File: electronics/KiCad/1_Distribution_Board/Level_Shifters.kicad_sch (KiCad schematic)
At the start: 39 parts, among them J16 Conn_01x02, J2 Conn_01x02, J24 Conn_01x03, J25 Conn_01x03, J26 Conn_01x03, J27 Conn_01x03, Q1 TBD, Q10 2N7000, Q4 TBD, Q6 2N7000, Q7 2N7000, Q8 2N7000, Q9 2N7000

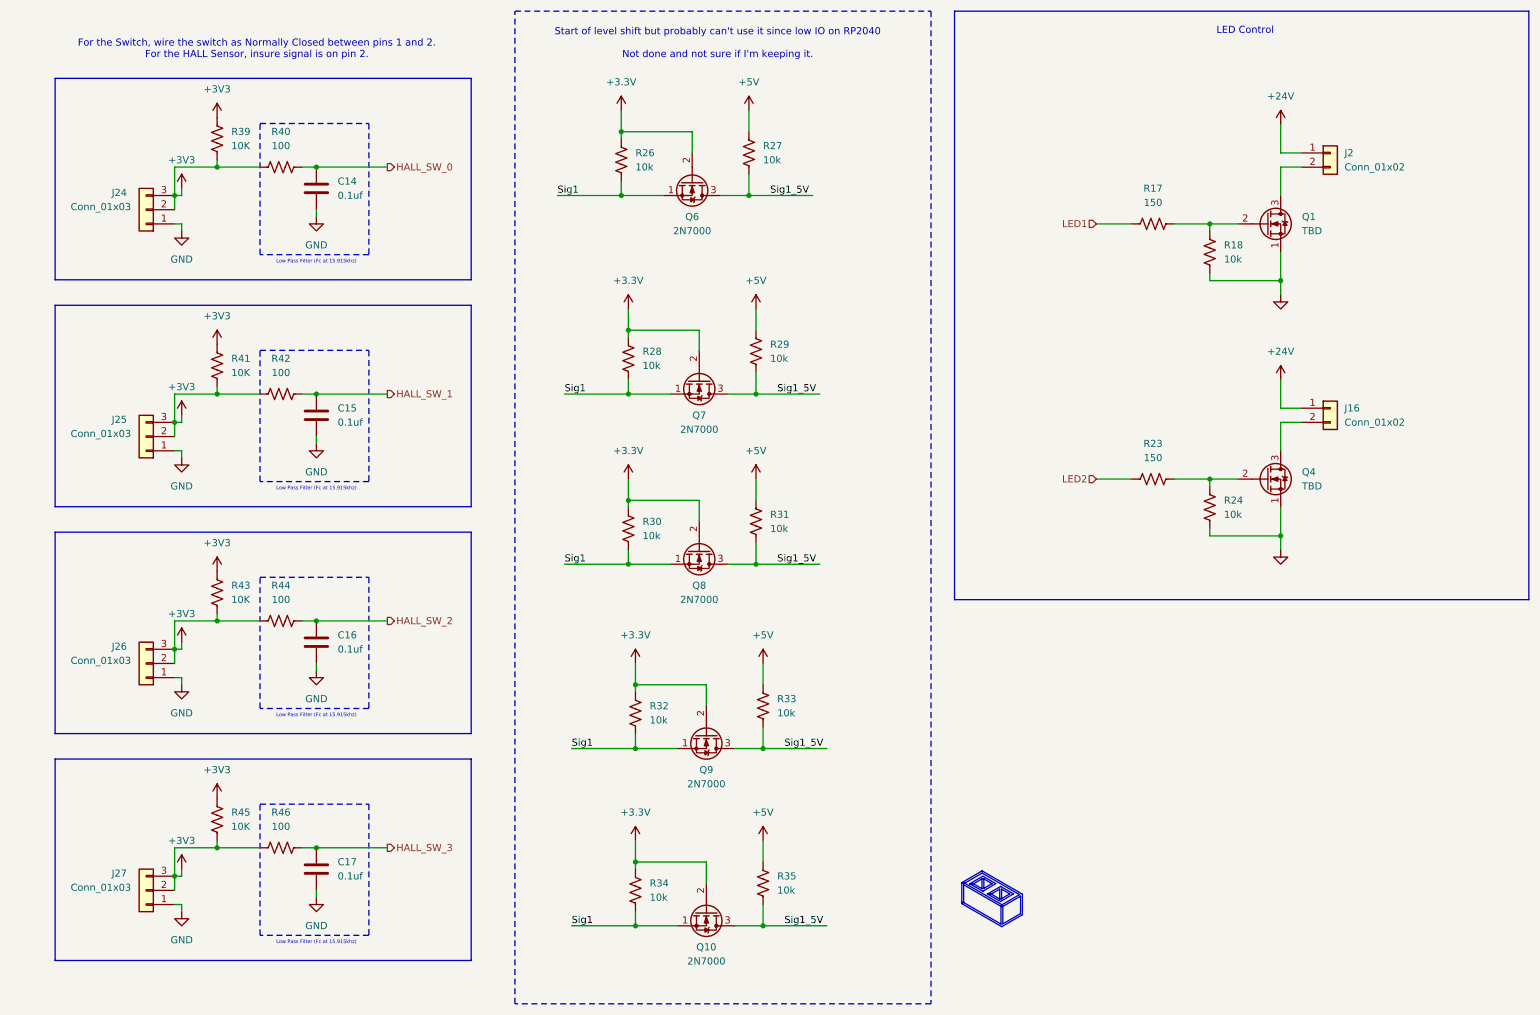
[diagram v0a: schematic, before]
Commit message: Updated schematics
Updated to remove additional stepper drive, corrected short on hall circuit. Removed level shifters for PWM signals.
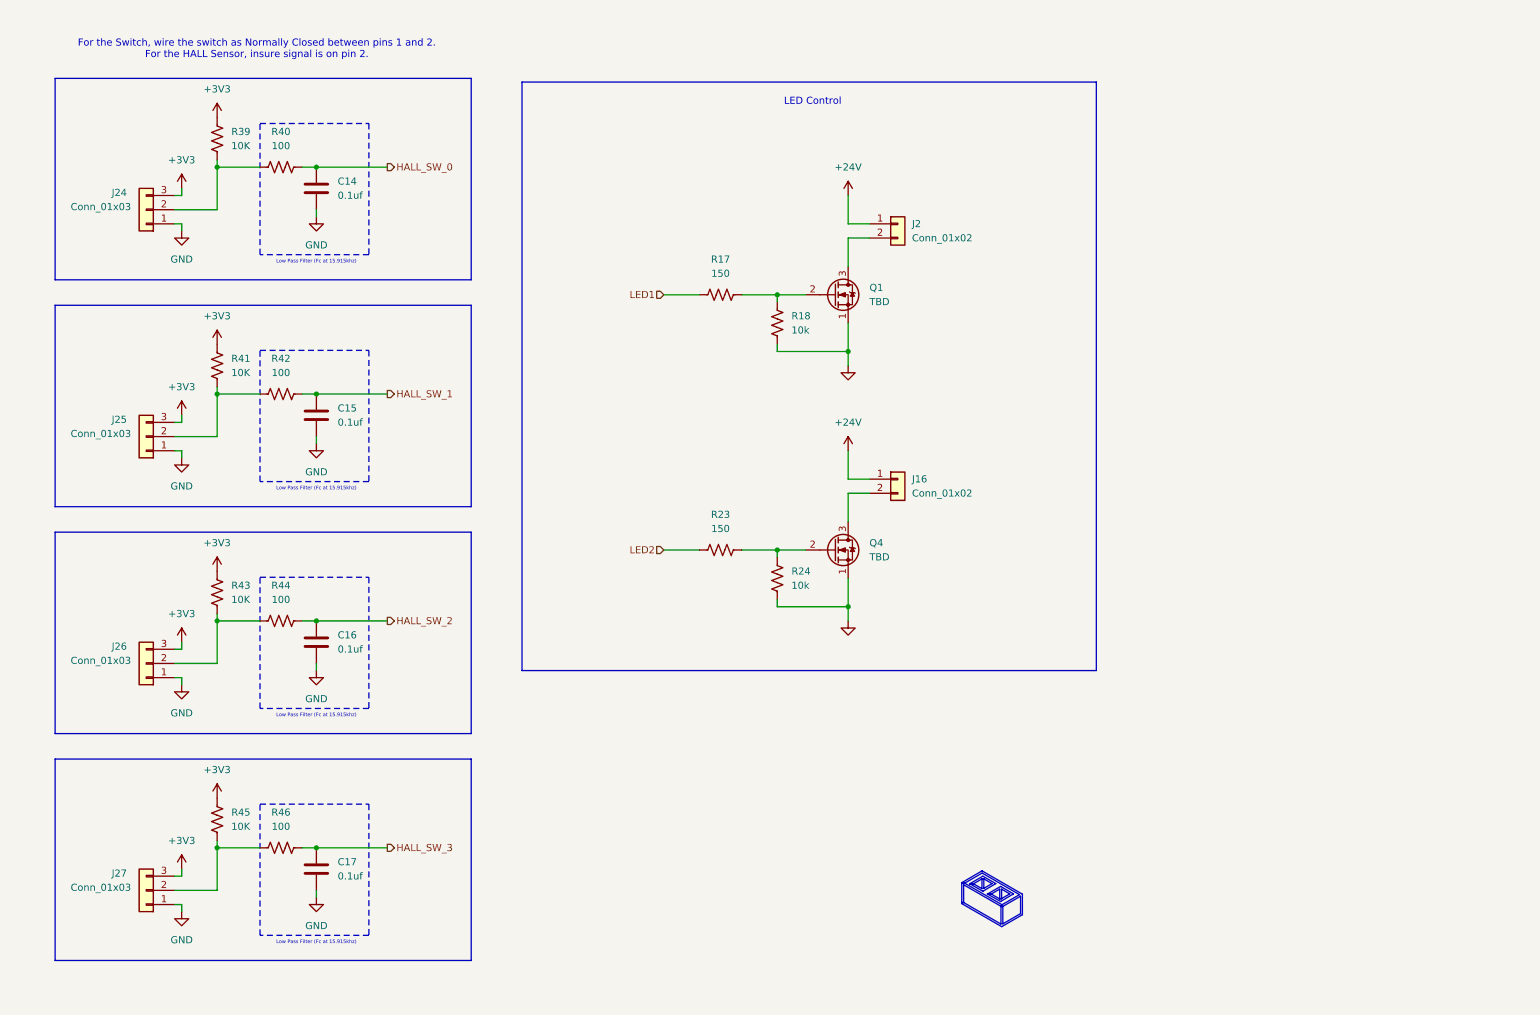
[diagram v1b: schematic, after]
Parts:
- removed Q10, Q6, Q7, Q8, Q9: 2N7000, Package_TO_SOT_THT:TO-92_Inline, symbol Transistor_FET:2N7000
- removed R26, R27, R28, R29, R30, R31, R32, R33, R34, R35: 10k, symbol Device:R_US
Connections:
- net +3V3: no longer J24.2 (Pin_2), J25.2 (Pin_2), J26.2 (Pin_2), J27.2 (Pin_2), R39.2, R40.1, R41.2, R42.1, R43.2, R44.1, R45.2, R46.1
- new net: J25.2 (Pin_2), R41.2, R42.1
- new net: J26.2 (Pin_2), R43.2, R44.1
- new net: J24.2 (Pin_2), R39.2, R40.1
- new net: J27.2 (Pin_2), R45.2, R46.1
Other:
- note removed: "Start of level shift but probably can't use it since low IO on RP2040 Not done and not sure if I'm keeping it."
- moved on the sheet: J16, J2, Q1, Q4, R17, R18, R23, R24

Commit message: footprint additions
Added Footprints to resistors and most components.
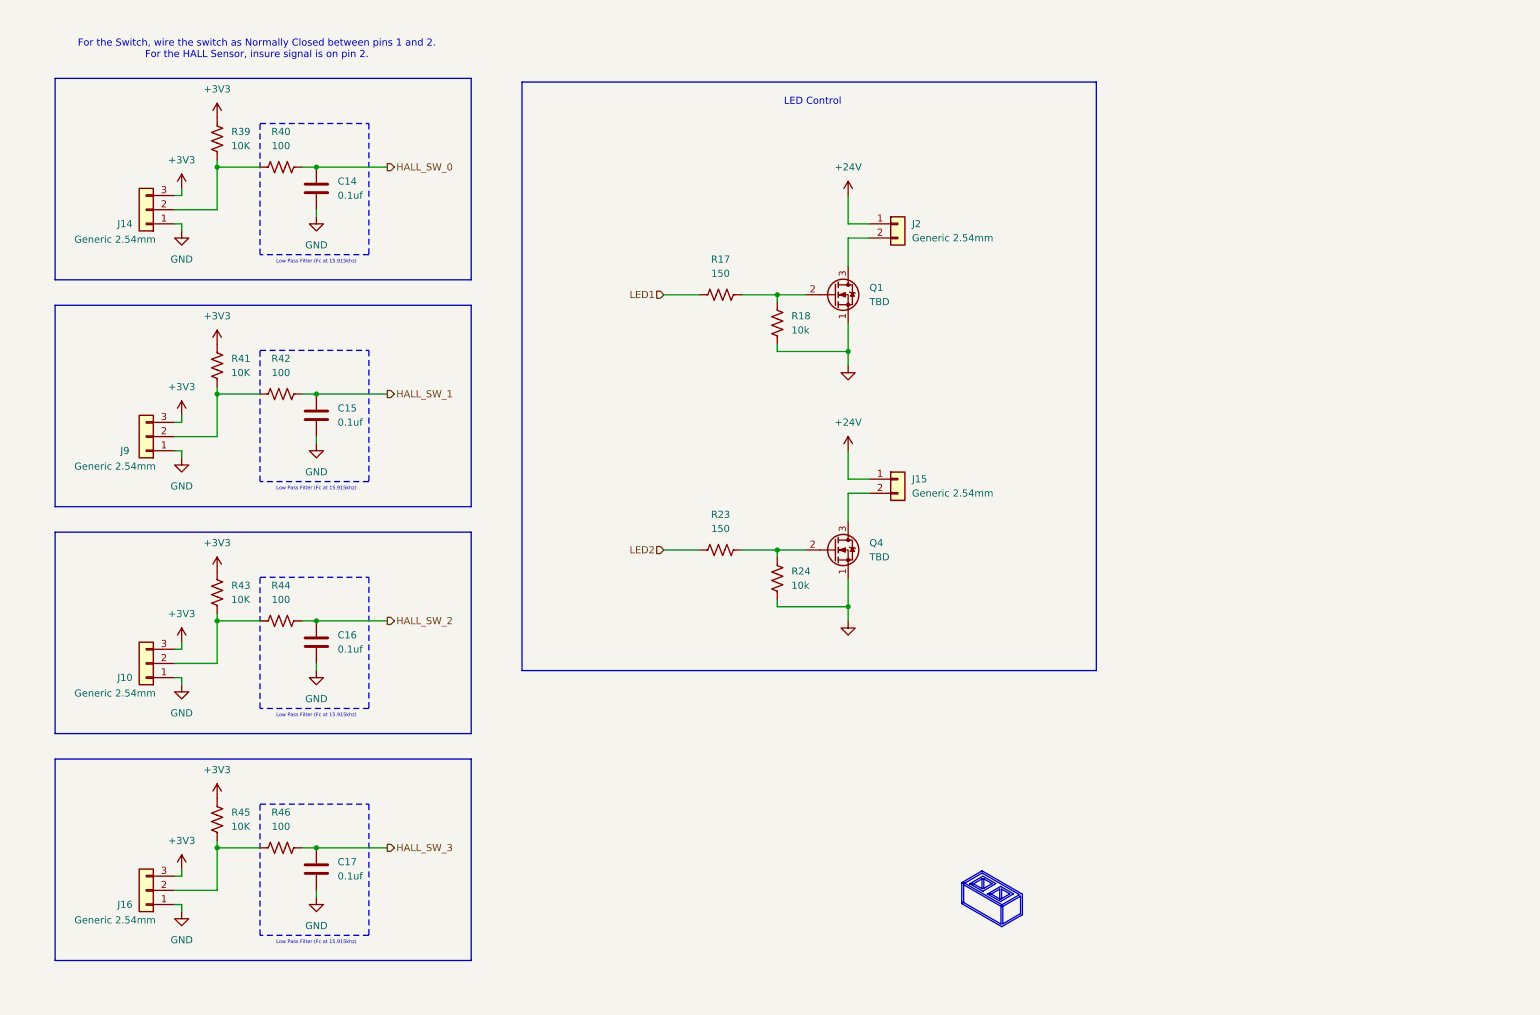
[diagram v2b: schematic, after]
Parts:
- removed J16: Conn_01x02, symbol Connector_Generic:Conn_01x02
- removed J24, J25, J26, J27: Conn_01x03, symbol Connector_Generic:Conn_01x03
- added J10, J14, J16, J9: Generic 2.54mm, Connector_PinHeader_2.54mm:PinHeader_1x03_P2.54mm_Vertical, symbol Connector_Generic:Conn_01x03
- added J15: Generic 2.54mm, Connector_PinHeader_2.54mm:PinHeader_1x02_P2.54mm_Vertical, symbol Connector_Generic:Conn_01x02
- C14, C15, C16, C17: footprint (none) -> Capacitor_SMD:C_0805_2012Metric_Pad1.18x1.45mm_HandSolder
- J2: value Conn_01x02 -> Generic 2.54mm; footprint (none) -> Connector_PinHeader_2.54mm:PinHeader_1x02_P2.54mm_Vertical
- R17, R18, R23, R24, R39, R40, R41, R42, R43, R44, R45, R46: footprint (none) -> Resistor_SMD:R_0805_2012Metric_Pad1.20x1.40mm_HandSolder
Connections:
- net +24V: now also J15.1 (Pin_1)
- net +3V3: now also J10.3 (Pin_3), J14.3 (Pin_3), J16.3 (Pin_3), J9.3 (Pin_3)
- net GND: now also J10.1 (Pin_1), J14.1 (Pin_1), J16.1 (Pin_1), J9.1 (Pin_1)
- net at R41.2, R42.1: now also J9.2 (Pin_2)
- net at R43.2, R44.1: now also J10.2 (Pin_2)
- net at R39.2, R40.1: now also J14.2 (Pin_2)
- net at Q4.3 (D): now also J15.2 (Pin_2)
- net at R45.2, R46.1: now also J16.2 (Pin_2)

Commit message: Updated to add 2 more steppers
Updated to add two more steppers, dual with the motor controllers. they will be either or. Layout hole pattern started. Still need some footprints assigned.
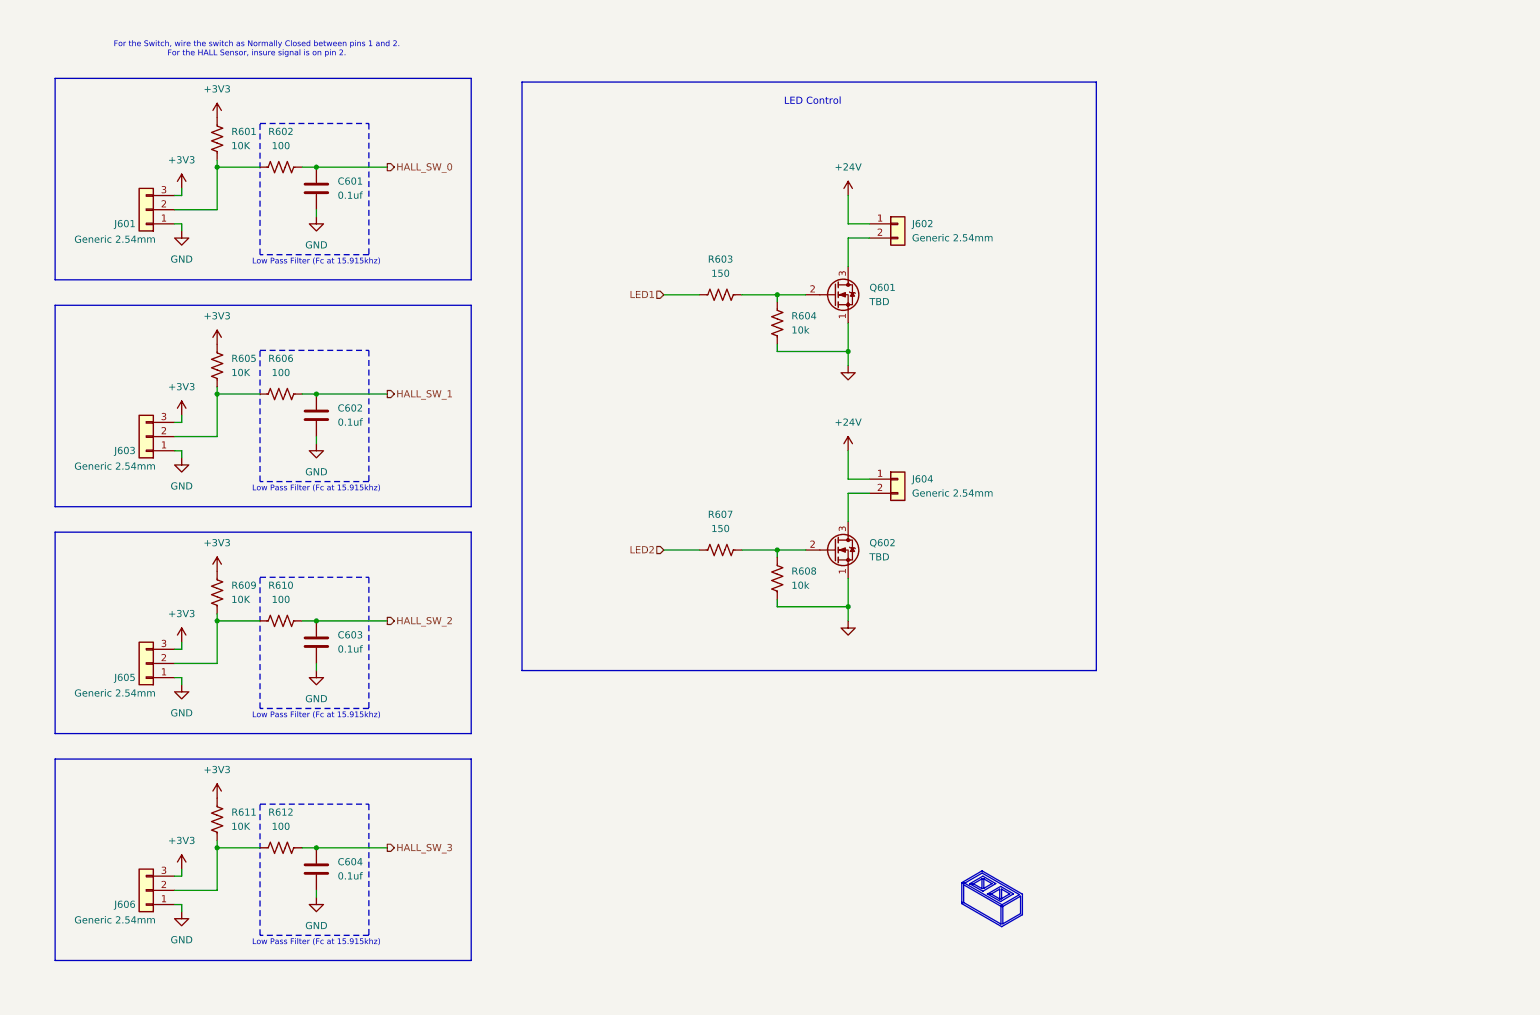
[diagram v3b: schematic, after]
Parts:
- renumbered C14 to C601, C15 to C602, C16 to C603, C17 to C604, J14 to J601, J2 to J602, J9 to J603, J15 to J604, J10 to J605, J16 to J606, Q1 to Q601, Q4 to Q602, R39 to R601, R40 to R602, R17 to R603, R18 to R604, R41 to R605, R42 to R606, R23 to R607, R24 to R608, R43 to R609, R44 to R610, R45 to R611, R46 to R612

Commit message: Added 4th stepper
Added 4th stepper on SCH and PCB
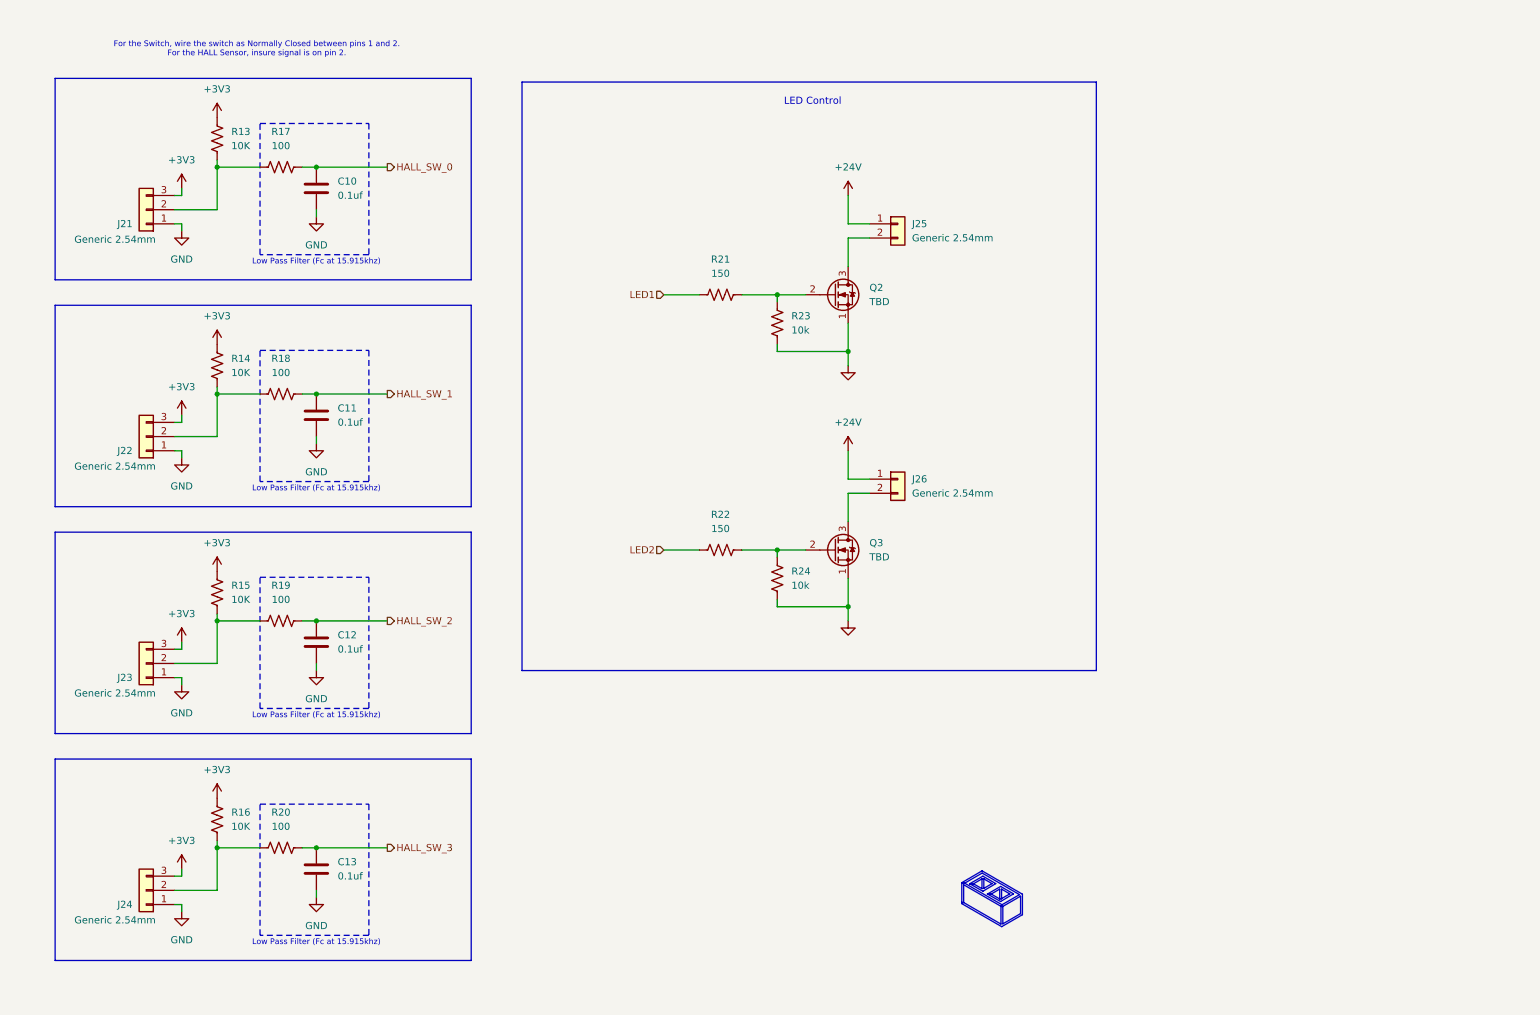
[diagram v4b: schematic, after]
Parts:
- renumbered C601 to C10, C602 to C11, C603 to C12, C604 to C13, J601 to J21, J603 to J22, J605 to J23, J606 to J24, J602 to J25, J604 to J26, Q601 to Q2, Q602 to Q3, R601 to R13, R605 to R14, R609 to R15, R611 to R16, R602 to R17, R606 to R18, R610 to R19, R612 to R20, R603 to R21, R607 to R22, R604 to R23, R608 to R24

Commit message: Updated sch
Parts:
- added J101, J601: Conn_01x04, symbol Connector_Generic:Conn_01x04
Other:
- note added: "NEO Pixel 1"
- note added: "NEO Pixel 2"
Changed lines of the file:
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@@
+	)
+	(rectangle
+		(start 208.915 26.67)
+		(end 278.13 67.31)
+		(stroke
+			(width 0)
+			(type solid)
+		)
+		(fill
+			(type none)
+		)
 	)
 	(rectangle
@@
 			(width 0)
 			(type dot)
+		)
+		(fill
+			(type none)
+		)
+	)
+	(rectangle
+		(start 208.915 69.85)
+		(end 278.13 110.49)
+		(stroke
+			(width 0)
+			(type solid)
 		)
 		(fill
@@
 		)
 	)
+	(text "NEO Pixel 2"
+		(exclude_from_sim no)
+		(at 243.078 75.438 0)
+		(effects
+			(font
+				(size 1.27 1.27)
+			)
+		)
+	)
 	(text "For the Switch, wire the switch as Normally Closed between pins 1 and 2.\nFor the HALL Sensor, insure signal is on pin 2.\n"
 		(exclude_from_sim no)
@@
 			(font
 				(size 1.016 1.016)
+			)
+		)
+	)
+	(text "NEO Pixel 1"
+		(exclude_from_sim no)
+		(at 243.078 32.258 0)
+		(effects
+			(font
+				(size 1.27 1.27)
 			)
 		)
@@
 	)
 	(symbol
+		(lib_id "Connector_Generic:Conn_01x04")
+		(at 255.27 91.44 0)
+		(unit 1)
+		(exclude_from_sim no)
+		(in_bom yes)
+		(on_board yes)
+		(dnp no)
+		(fields_autoplaced yes)
+		(property "Reference" "J601"
+			(at 257.81 91.4399 0)
+			(effects
+				(font
+					(size 1.27 1.27)
+				)
+				(justify left)
+			)
+		)
+		(property "Value" "Conn_01x04"
+			(at 257.81 93.9799 0)
+			(effects
+				(font
+					(size 1.27 1.27)
+				)
+				(justify left)
+			)
+		)
+		(property "Footprint" ""
+			(at 255.27 91.44 0)
+			(effects
+				(font
+					(size 1.27 1.27)
+				)
+				(hide yes)
+			)
+		)
+		(property "Datasheet" "~"
+			(at 255.27 91.44 0)
+			(effects
+				(font
+					(size 1.27 1.27)
+				)
+				(hide yes)
+			)
+		)
+		(property "Description" "Generic connector, single row, 01x04, script generated (kicad-library-utils/schlib/autogen/connector/)"
+			(at 255.27 91.44 0)
+			(effects
+				(font
+					(size 1.27 1.27)
+				)
+				(hide yes)
+			)
+		)
+		(pin "2"
+		)
+		(pin "4"
+		)
+		(pin "3"
+		)
+		(pin "1"
+		)
+		(instances
+			(project "1_Distribution_Board"
+				(path "/d53c8c01-e754-4310-8a73-7d7c95e64cd3/aa124a9b-4ca6-4e8b-864b-f6c7e5891937"
+					(reference "J601")
+					(unit 1)
+				)
+			)
+		)
+	)
+	(symbol
 		(lib_id "Device:R_US")
 		(at 137.16 64.77 90)
@@
 					(unit 1)
 				)
+			)
+		)
+	)
+	(symbol
+		(lib_id "Connector_Generic:Conn_01x04")
+		(at 255.27 48.26 0)
+		(unit 1)
+		(exclude_from_sim no)
+		(in_bom yes)
+		(on_board yes)
+		(dnp no)
+		(fields_autoplaced yes)
+		(property "Reference" "J101"
+			(at 257.81 48.2599 0)
+			(effects
+				(font
+					(size 1.27 1.27)
+				)
+				(justify left)
+			)
+		)
+		(property "Value" "Conn_01x04"
+			(at 257.81 50.7999 0)
+			(effects
+				(font
+					(size 1.27 1.27)
+				)
+				(justify left)
+			)
+		)
+		(property "Footprint" ""
+			(at 255.27 48.26 0)
+			(effects
+				(font
+					(size 1.27 1.27)
+				)
+				(hide yes)
+			)
+		)
+		(property "Datasheet" "~"
+			(at 255.27 48.26 0)
+			(effects
+				(font
+					(size 1.27 1.27)
+				)
+				(hide yes)
+			)
+		)
+		(property "Description" "Generic connector, single row, 01x04, script generated (kicad-library-utils/schlib/autogen/connector/)"
+			(at 255.27 48.26 0)
+			(effects
+				(font
+					(size 1.27 1.27)
+				)
+				(hide yes)
+			)
+		)
+		(pin "2"
+		)
+		(pin "4"
+		)
+		(pin "3"
+		)
+		(pin "1"
+		)
+		(instances
+			(project "1_Distribution_Board"
+				(path "/d53c8c01-e754-4310-8a73-7d7c95e64cd3/aa124a9b-4ca6-4e8b-864b-f6c7e5891937"
+					(reference "J101")
+					(unit 1)
+				)
